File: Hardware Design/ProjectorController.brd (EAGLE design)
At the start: 55.5 x 38.1 mm, 13 parts, among them J1 5747844-4, J2 Cap Buttons, J3 Prog, J4 Prog/Run, J5 10118194-0001LF, U1 ESP-WROOM-32, U2 SP3232EEN-L

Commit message: Progress on board layout PC-13
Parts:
- added C3, C4, C5, C6, C7: 0.1uF, SparkFun-Capacitors:1206
- moved S1 39.9 mm to (41.9, 49.5), turned to 270 degrees
- moved R2 39.4 mm to (19.1, 66.0)
- moved J4 32.9 mm to (13.5, 60.7)
- moved R1 16.2 mm to (30.5, 48.4), flipped to the bottom, turned to 90 degrees
- moved J2 7.62 mm to (48.3, 71.1)
- moved J1 5.08 mm to (21.6, 69.8)
- moved U2 5.08 mm to (44.5, 62.2), turned to 90 degrees
- moved U1 3.81 mm to (26.7, 53.3)
- moved C2 3.18 mm to (12.1, 57.0)
- moved U$1 3.05 mm to (8.38, 63.6)
- moved C1 1.77 mm to (6.99, 55.5), flipped to the bottom, turned to 0 degrees
- moved J3 1.27 mm to (12.7, 45.7)
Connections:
- removed net V+: U2.2
- removed net V-: U2.6
- new net N$12: C5.2, U2.1
- new net N$14: C5.1, U2.3
- new net N$15: C4.2, U2.4
- new net N$16: C4.1, U2.5
- new net N$17: C7.2, U2.2
- new net N$19: C6.2, U2.6
- net 3V3: now also C3.2
- net GND: now also C3.1, C6.1, C7.1
- net N$7: now also J3.2; no longer J3.3
- net N$8: now also J3.3; no longer J3.2
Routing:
- net 3V3: track 0.00 -> 65.3 mm, vias 0 -> 3
- net GND: track 0.00 -> 48.8 mm, vias 0 -> 2
- net N$4: track 0.00 -> 15.4 mm, vias 0 -> 1
- net N$9: track 0.00 -> 13.5 mm
- net 5V: track 0.00 -> 11.1 mm
- net N$13: track 0.00 -> 9.58 mm
- net N$16: track 0.00 -> 4.83 mm
- net N$12: track 0.00 -> 4.30 mm
- net N$15: track 0.00 -> 4.20 mm
- net N$14: track 0.00 -> 4.20 mm
- net N$7: track 0.00 -> 0.64 mm
- net N$8: track 0.00 -> 0.63 mm
- added copper zone on layer 16, net GND
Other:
- board size 55.5 x 38.1 mm -> 46.7 x 38.1 mm

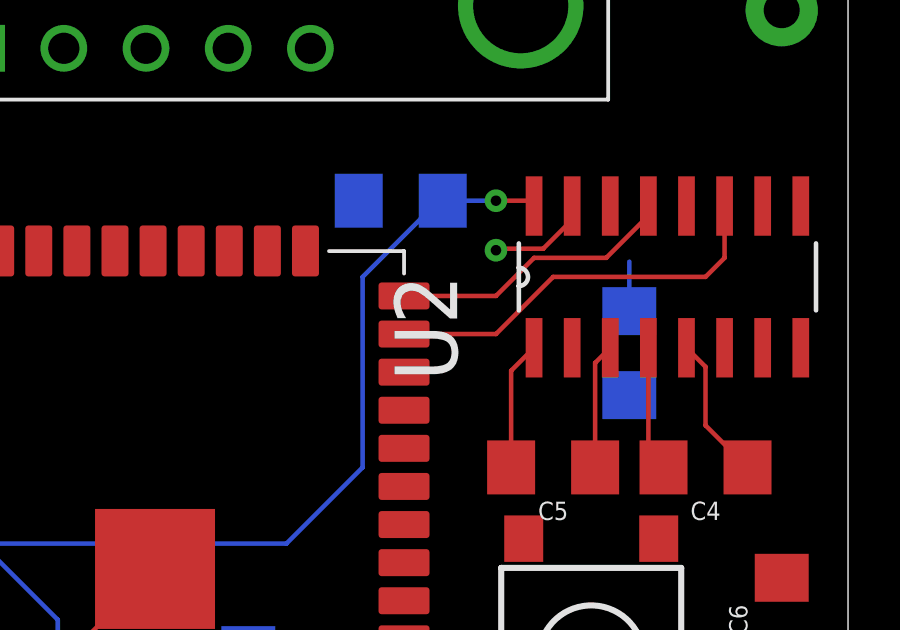
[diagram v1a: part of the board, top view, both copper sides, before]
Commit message: Switched UART Pins PC-12
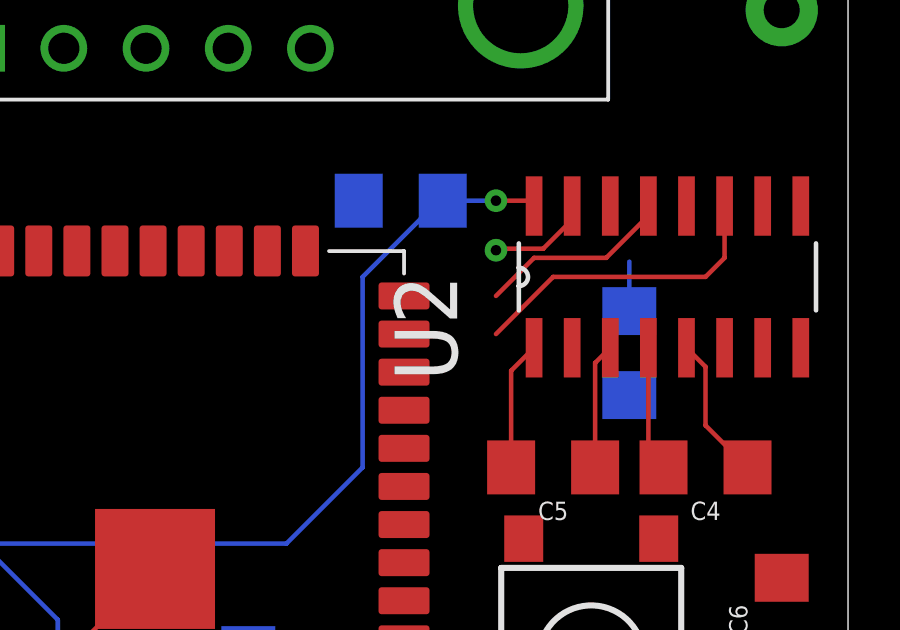
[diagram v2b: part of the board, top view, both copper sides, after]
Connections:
- net N$13: now also U1.27; no longer U1.14
- net N$9: now also U1.28; no longer U1.13
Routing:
- net N$13: track 9.58 -> 6.51 mm
- net N$9: track 13.5 -> 10.4 mm
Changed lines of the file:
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@@
 </signal>
 <signal name="N$13">
-<contactref element="U1" pad="14"/>
 <contactref element="U2" pad="13"/>
-<wire x1="35.67" y1="61.595" x2="38.735" y2="61.595" width="0.1524" layer="1"/>
 <wire x1="42.4110875" y1="62.865" x2="43.815" y2="64.2689125" width="0.1524" layer="1"/>
 <wire x1="43.815" y1="64.2689125" x2="43.815" y2="64.5922" width="0.1524" layer="1"/>
 <wire x1="38.735" y1="61.595" x2="40.005" y2="62.865" width="0.1524" layer="1"/>
 <wire x1="40.005" y1="62.865" x2="42.4110875" y2="62.865" width="0.1524" layer="1"/>
+<contactref element="U1" pad="27"/>
+<wire x1="17.67" y1="59.055" x2="38.735" y2="61.595" width="0" layer="19" extent="1-1"/>
 </signal>
 <signal name="N$9">
 <contactref element="U2" pad="11"/>
-<contactref element="U1" pad="13"/>
-<wire x1="35.67" y1="60.325" x2="38.735" y2="60.325" width="0.1524" layer="1"/>
 <wire x1="38.735" y1="60.325" x2="40.64" y2="62.23" width="0.1524" layer="1"/>
 <wire x1="40.64" y1="62.23" x2="45.72" y2="62.23" width="0.1524" layer="1"/>
 <wire x1="45.72" y1="62.23" x2="46.355" y2="62.865" width="0.1524" layer="1"/>
 <wire x1="46.355" y1="62.865" x2="46.355" y2="64.5922" width="0.1524" layer="1"/>
+<contactref element="U1" pad="28"/>
+<wire x1="17.67" y1="57.785" x2="38.735" y2="60.325" width="0" layer="19" extent="1-1"/>
 </signal>
 <signal name="N$12">

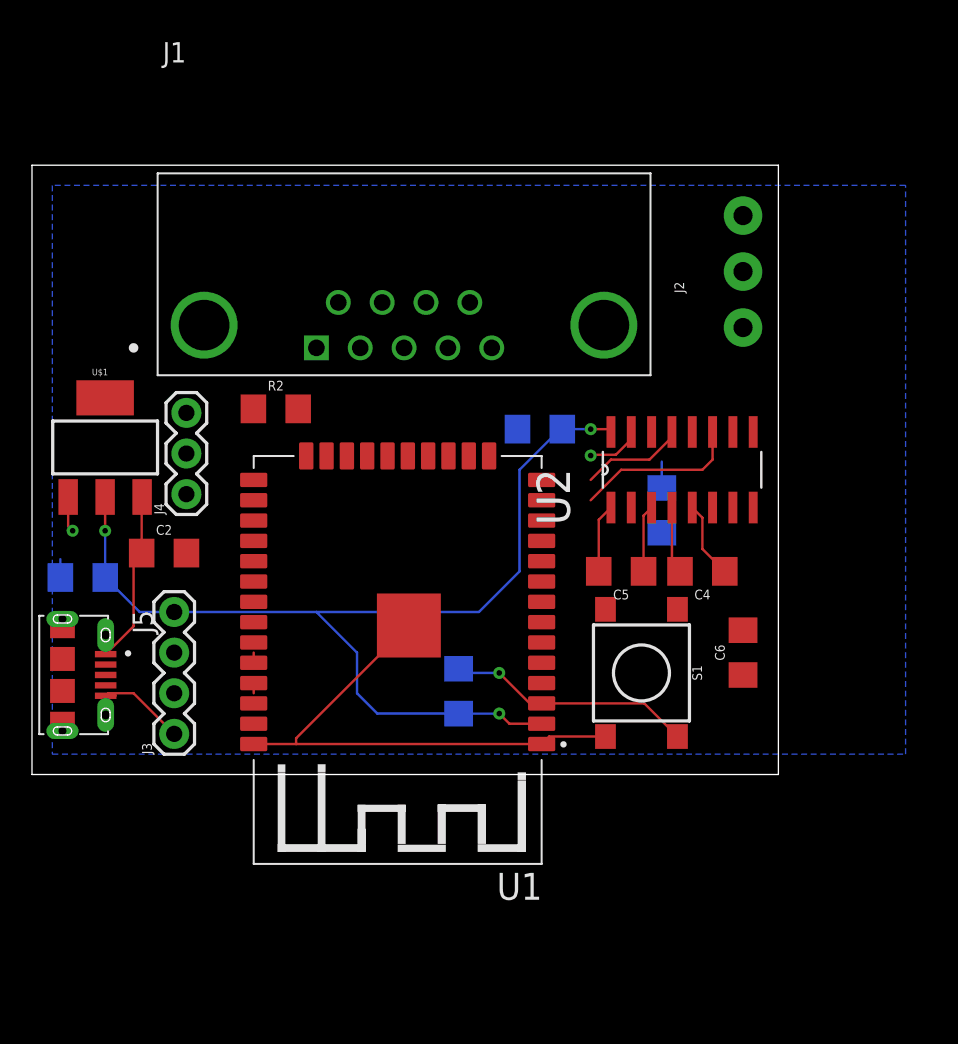
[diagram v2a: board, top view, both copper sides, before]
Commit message: Board Layout Complete PC-13
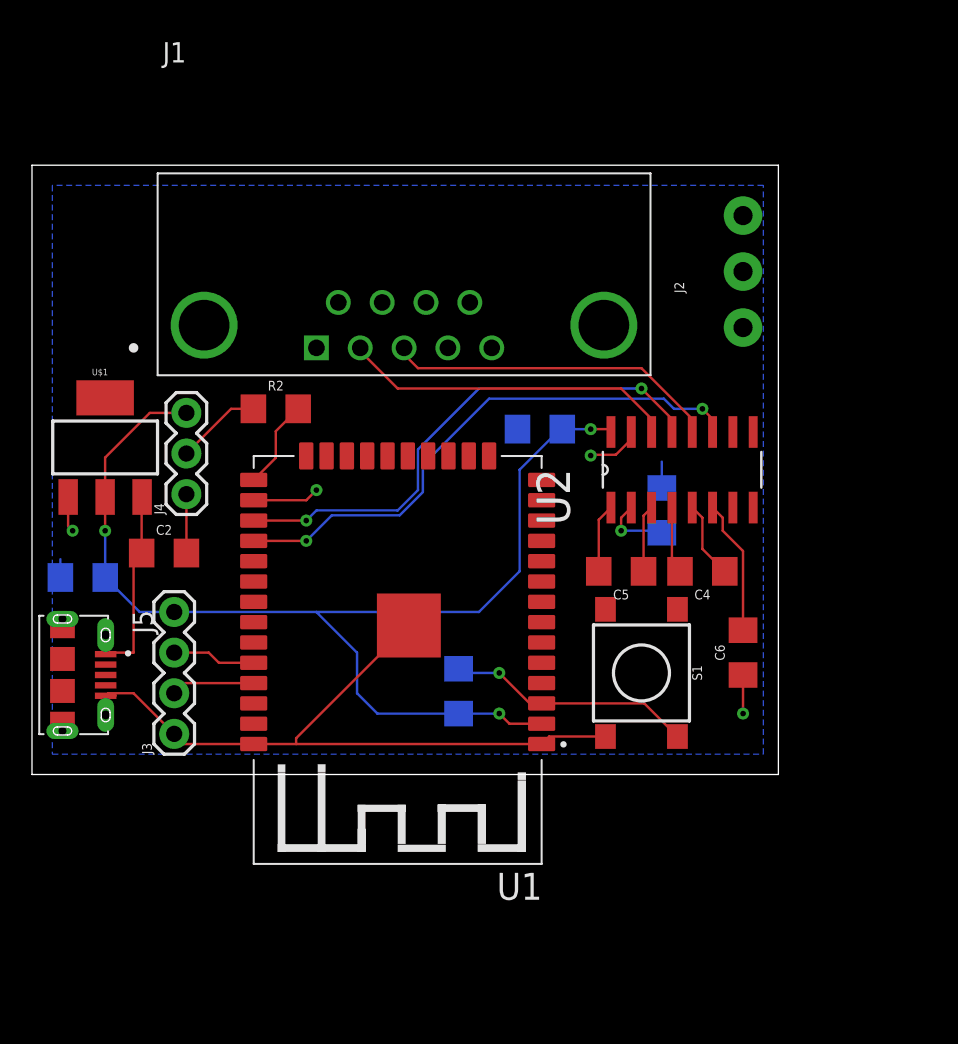
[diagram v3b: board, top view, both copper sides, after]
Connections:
- net N$1: now also J2.3; no longer J2.1
- net N$2: now also J2.1; no longer J2.2
- net N$3: now also J2.2; no longer J2.3
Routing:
- net N$13: track 6.51 -> 33.0 mm, vias 0 -> 2
- net N$9: track 10.4 -> 34.7 mm, vias 0 -> 2
- net N$10: track 0.00 -> 21.0 mm
- net N$11: track 0.00 -> 20.9 mm
- net GND: track 48.8 -> 60.1 mm, vias 2 -> 3
- net 3V3: track 65.3 -> 74.0 mm
- net N$19: track 0.00 -> 8.46 mm
- net N$5: track 0.00 -> 5.60 mm
- net N$6: track 0.00 -> 5.35 mm
- net N$8: track 0.63 -> 5.23 mm
- net N$7: track 0.64 -> 5.23 mm
- net N$17: track 0.00 -> 4.30 mm, vias 0 -> 1
- net N$3: track 0.00 -> 4.18 mm, vias 0 -> 1
- net 5V: track 11.1 -> 11.9 mm

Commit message: Optimised Layout
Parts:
- C1, C2: value (none) -> 10uF
- moved C6 31.7 mm to (16.5, 50.8), flipped to the bottom
- moved C4 27.1 mm to (19.1, 50.8), flipped to the bottom, turned to 270 degrees
- moved C7 21.0 mm to (24.1, 50.8), turned to 90 degrees
- moved U2 20.7 mm to (24.1, 58.4), flipped to the bottom
- moved C5 19.7 mm to (21.6, 50.8), flipped to the bottom, turned to 270 degrees
- moved J2 17.4 mm to (40.0, 55.8)
- moved S1 9.25 mm to (33.0, 52.1), flipped to the bottom
- moved J1 5.68 mm to (16.5, 67.3)
- moved R1 4.58 mm to (26.7, 50.9)
- moved U$1 4.57 mm to (8.38, 59.1)
- moved C2 4.32 mm to (8.26, 59.1), flipped to the bottom
- moved C3 3.59 mm to (33.0, 62.2), turned to 0 degrees
- moved R2 2.54 mm to (19.1, 63.5), flipped to the bottom, turned to 180 degrees
- moved U1 1.27 mm to (25.4, 53.3)
- moved C1 1.27 mm to (8.26, 55.5)
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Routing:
- net N$9: track 34.7 -> 9.28 mm, vias 2 -> 1
- net N$13: track 33.0 -> 10.1 mm, vias 2 -> 1
- net N$3: track 4.18 -> 25.7 mm, vias 1 -> 0
- net N$1: track 0.00 -> 21.0 mm
- net GND: track 60.1 -> 44.2 mm, vias 3 -> 2
- net N$11: track 20.9 -> 7.15 mm
- net 3V3: track 74.0 -> 63.9 mm, vias 3 -> 2
- net N$10: track 21.0 -> 13.2 mm
- net N$12: track 4.30 -> 11.9 mm
- net N$15: track 4.20 -> 10.5 mm
- net N$2: track 0.00 -> 5.88 mm
- net N$4: track 15.4 -> 11.2 mm
- net N$14: track 4.20 -> 7.19 mm
- net N$16: track 4.83 -> 7.19 mm
- net N$6: track 5.35 -> 7.42 mm
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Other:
- board size 46.7 x 38.1 mm -> 39 x 34.9 mm

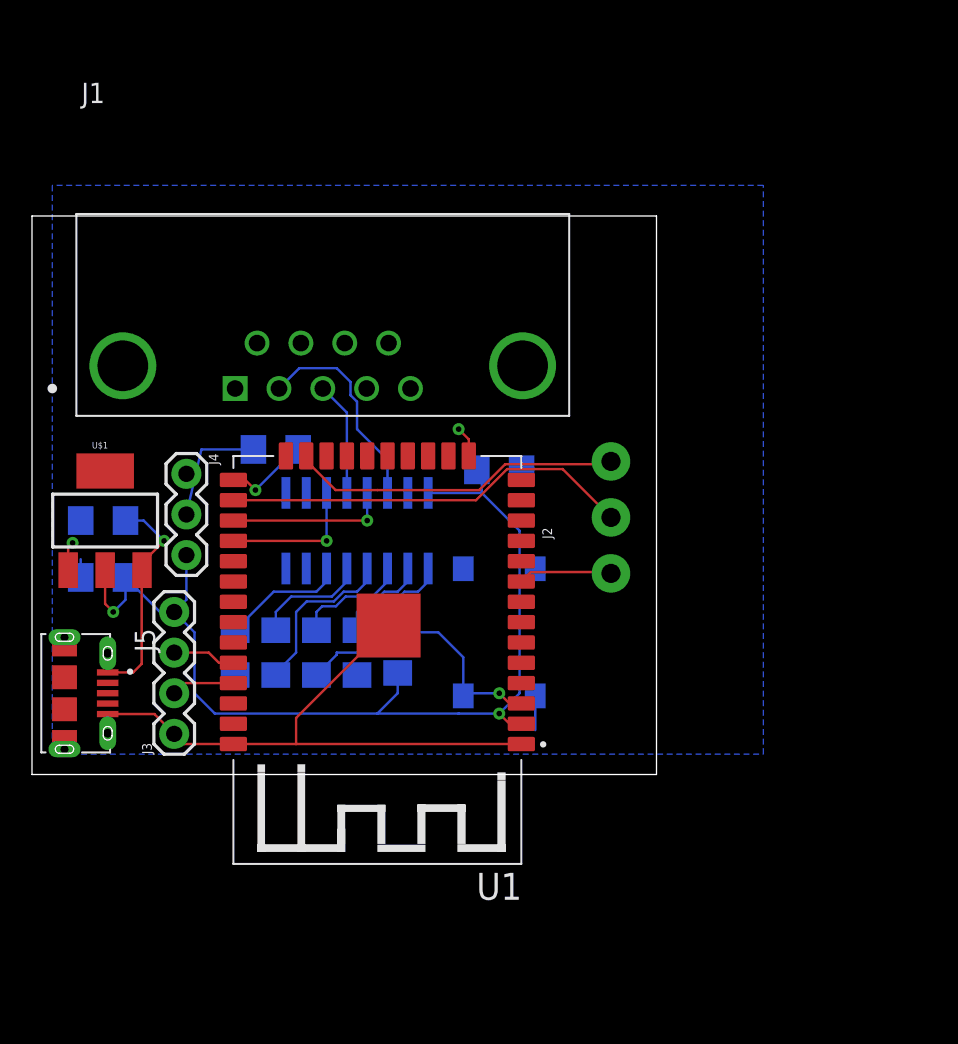
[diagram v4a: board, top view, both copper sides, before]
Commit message: Revert "Revert "ED-33 Major board redesign to make smaller""
This reverts commit 3ae201e74c16ce24ee355c7bdbcad0014f833ec8.
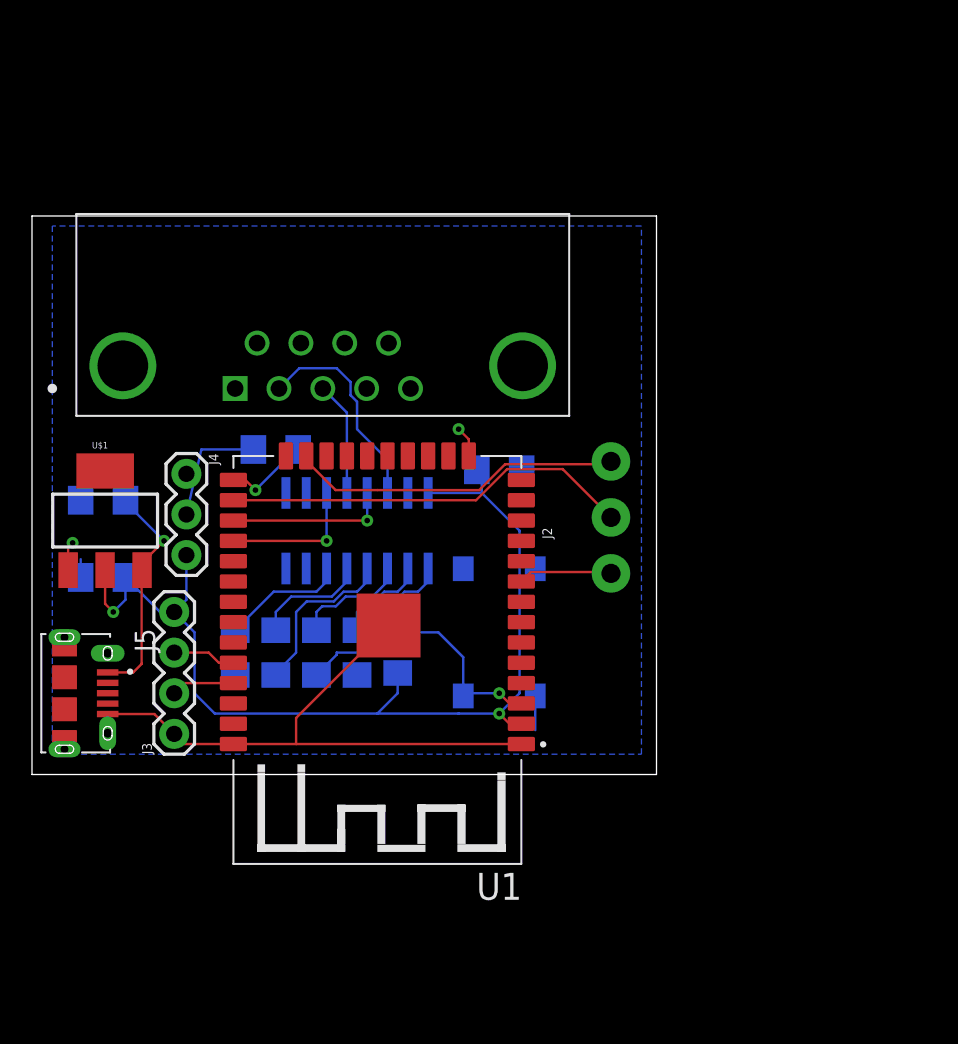
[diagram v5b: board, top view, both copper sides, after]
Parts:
- moved C2 1.27 mm to (8.26, 60.3)
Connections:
- net GND: now also J5.S1, J5.S2, J5.S3, J5.S4, J5.S5, J5.S6
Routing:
- net 5V: track 13.6 -> 14.2 mm
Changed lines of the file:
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@@
 <?xml version="1.0" encoding="utf-8"?>
 <!DOCTYPE eagle SYSTEM "eagle.dtd">
-<eagle version="9.5.2">
+<eagle version="9.6.1">
 <drawing>
 <settings>
@@
 <attribute name="VALUE" x="8.255" y="54.356" size="0.6096" layer="28" font="vector" ratio="20" rot="MR0" align="top-center"/>
 </element>
-<element name="C2" library="SparkFun-Capacitors" package="1206" value="10uF" x="8.255" y="59.055" smashed="yes" rot="MR0">
-<attribute name="NAME" x="8.255" y="60.198" size="0.6096" layer="26" font="vector" ratio="20" rot="MR0" align="bottom-center"/>
-<attribute name="VALUE" x="8.255" y="57.912" size="0.6096" layer="28" font="vector" ratio="20" rot="MR0" align="top-center"/>
+<element name="C2" library="SparkFun-Capacitors" package="1206" value="10uF" x="8.255" y="60.325" smashed="yes" rot="MR0">
+<attribute name="NAME" x="8.255" y="61.468" size="0.6096" layer="26" font="vector" ratio="20" rot="MR0" align="bottom-center"/>
+<attribute name="VALUE" x="8.255" y="59.182" size="0.6096" layer="28" font="vector" ratio="20" rot="MR0" align="top-center"/>
 </element>
 <element name="J1" library="5747844-4" package="TE_5747844-4" value="5747844-4" x="16.51" y="67.31" smashed="yes">
@@
 <attribute name="MF" value="TE Connectivity" x="54.61" y="29.21" size="1.778" layer="27" display="off"/>
 <attribute name="MP" value="5747844-4" x="54.61" y="29.21" size="1.778" layer="27" display="off"/>
-<attribute name="NAME" x="6.90275" y="85.152" size="1.27228125" layer="25"/>
 <attribute name="NUMBER_OF_POSITIONS" value="9" x="54.61" y="29.21" size="1.778" layer="27" display="off"/>
 <attribute name="PACKAGE" value="None" x="54.61" y="29.21" size="1.778" layer="27" display="off"/>
@@
 <element name="J2" library="SparkFun-Connectors" package="SCREWTERMINAL-3.5MM-3-NS" value="Cap Buttons" x="40.005" y="55.753" smashed="yes" rot="R90">
 <attribute name="NAME" x="36.322" y="57.912" size="0.6096" layer="25" font="vector" ratio="20" rot="R90"/>
-<attribute name="VALUE" x="44.577" y="57.785" size="0.6096" layer="27" font="vector" ratio="20" rot="R90"/>
+<attribute name="VALUE" x="38.227" y="57.785" size="0.6096" layer="27" font="vector" ratio="20" rot="R90"/>
 </element>
 <element name="J3" library="SparkFun-Connectors" package="1X04" value="Prog" x="12.7" y="45.72" smashed="yes" rot="R90">
@@
 <attribute name="PACKAGE" value="None" x="5.842" y="48.26" size="1.778" layer="27" rot="R270" display="off"/>
 <attribute name="PRICE" value="None" x="5.842" y="48.26" size="1.778" layer="27" rot="R270" display="off"/>
-<attribute name="VALUE" x="1.122040625" y="52.72785" size="1.270459375" layer="27" rot="R270"/>
 </element>
 <element name="C3" library="SparkFun-Capacitors" package="1206" value="0.1uF" x="33.02" y="62.23" smashed="yes" rot="MR0">
@@
 <contactref element="C7" pad="1"/>
 <polygon width="0.1524" layer="16">
-<vertex x="5.08" y="80.01"/>
+<vertex x="5.08" y="77.47"/>
 <vertex x="5.08" y="44.45"/>
-<vertex x="49.53" y="44.45"/>
-<vertex x="49.53" y="80.01"/>
+<vertex x="41.91" y="44.45"/>
+<vertex x="41.91" y="77.47"/>
 </polygon>
 <wire x1="6.855" y1="56.639" x2="6.855" y2="55.499" width="0.1524" layer="16"/>
@@
 <wire x1="6.0706" y1="55.9562" x2="6.0706" y2="57.3786" width="0.1524" layer="1"/>
 <wire x1="6.0706" y1="57.3786" x2="6.35" y2="57.658" width="0.1524" layer="1"/>
+<contactref element="J5" pad="S3"/>
+<contactref element="J5" pad="S6"/>
+<contactref element="J5" pad="S1"/>
+<contactref element="J5" pad="S2"/>
+<contactref element="J5" pad="S5"/>
+<contactref element="J5" pad="S4"/>
+<wire x1="5.842" y1="47.26" x2="5.842" y2="49.26" width="0" layer="19" extent="1-1"/>
+<wire x1="5.842" y1="51.76" x2="5.842" y2="49.26" width="0" layer="19" extent="1-1"/>
 </signal>
 <signal name="3V3">
@@
 <wire x1="10.665" y1="55.9278" x2="10.6934" y2="55.9562" width="0.1524" layer="1"/>
 <wire x1="8.542" y1="49.56" x2="8.572" y2="49.53" width="0.1524" layer="1"/>
-<wire x1="9.655" y1="59.055" x2="10.795" y2="59.055" width="0.1524" layer="16"/>
-<wire x1="12.065" y1="57.785" x2="10.795" y2="59.055" width="0.1524" layer="16"/>
+<wire x1="9.655" y1="60.325" x2="9.655" y2="60.195" width="0.1524" layer="16"/>
+<wire x1="12.065" y1="57.785" x2="9.655" y2="60.195" width="0.1524" layer="16"/>
 <via x="12.065" y="57.785" extent="1-16" drill="0.35"/>
 <wire x1="10.6934" y1="55.9562" x2="10.6934" y2="56.4134" width="0.1524" layer="1"/>
 <wire x1="12.065" y1="57.785" x2="10.6934" y2="56.4134" width="0.1524" layer="1"/>
-<wire x1="8.542" y1="49.56" x2="10.13" y2="49.56" width="0.1524" layer="1"/>
+<wire x1="8.542" y1="49.56" x2="10.13" y2="49.56" width="0.1524" layer="1" locked="yes"/>
 <wire x1="10.13" y1="49.56" x2="10.665" y2="50.095" width="0.1524" layer="1"/>
 <wire x1="10.665" y1="50.095" x2="10.665" y2="55.9278" width="0.1524" layer="1"/>
@@
 </board>
 </drawing>
+<compatibility>
+<note version="8.5" severity="warning">
+Since Version 8.5, EAGLE supports locking for holes, vias, wires and polygons.
+The locking property on all objects of these types will not be understood in this version.
+</note>
+</compatibility>
 </eagle>
